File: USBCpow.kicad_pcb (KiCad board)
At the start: 2 copper layers, 16.5 x 12.7 mm, 7 parts, among them CN1 CON_USB-C-6, J1 Conn_01x05, U1 LM1117-3.3

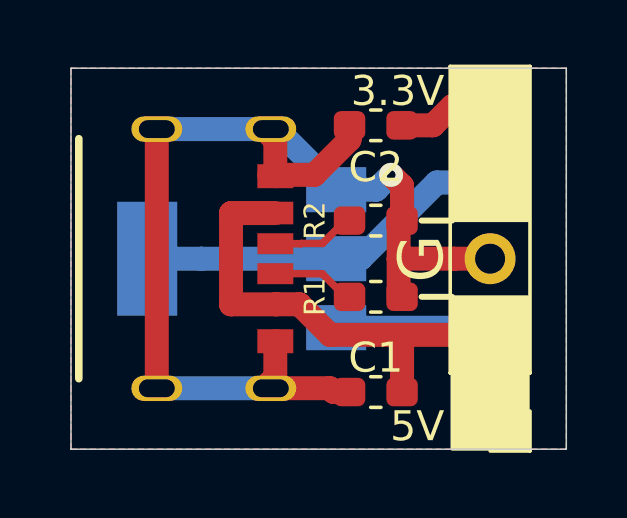
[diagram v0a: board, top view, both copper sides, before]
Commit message: 固定用ピンヘッダの穴を追加
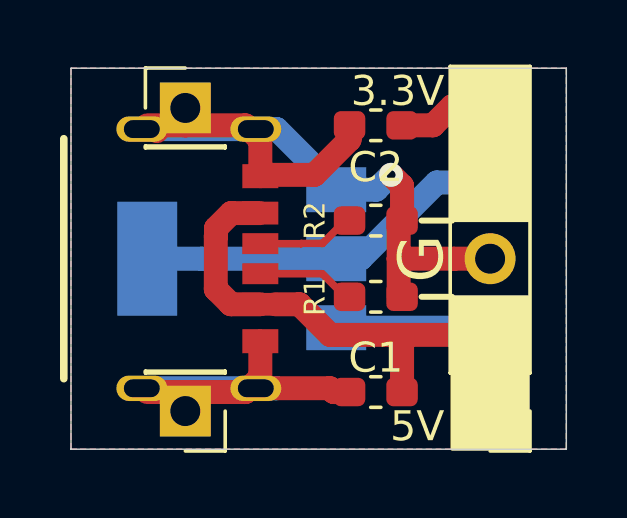
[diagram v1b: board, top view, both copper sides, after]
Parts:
- added J2: Conn_01x01, Connector_PinHeader_2.54mm:PinHeader_1x01_P2.54mm_Vertical, F.Cu at (3.81, -11.4)
- added J3: Conn_01x01, Connector_PinHeader_2.54mm:PinHeader_1x01_P2.54mm_Vertical, F.Cu at (3.81, -1.27)
- moved CN1 0.50 mm to (3.31, -6.35)
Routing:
- net Net-(C1-Pad1): track 25.9 -> 25.3 mm
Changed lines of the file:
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@@
     (thickness 1.6)
     (drawings 22)
-    (tracks 56)
+    (tracks 64)
     (zones 0)
-    (modules 7)
+    (modules 9)
     (nets 6)
   )
@@
   (layers
     (0 F.Cu signal hide)
-    (31 B.Cu signal)
+    (31 B.Cu signal hide)
     (32 B.Adhes user hide)
     (33 F.Adhes user hide)
@@
     (35 F.Paste user)
     (36 B.SilkS user)
-    (37 F.SilkS user)
+    (37 F.SilkS user hide)
     (38 B.Mask user)
-    (39 F.Mask user)
+    (39 F.Mask user hide)
     (44 Edge.Cuts user)
     (45 Margin user hide)
@@
   )
   (setup
-    (last_trace_width 0.25)
+    (last_trace_width 0.8)
     (user_trace_width 0.4)
     (user_trace_width 0.6)
@@
     (add_net "Net-(CN1-PadB5)")
   )
+  (module Connector_PinHeader_2.54mm:PinHeader_1x01_P2.54mm_Vertical (layer F.Cu)
+    (at 3.81 -1.27 180)
+    (descr "Through hole straight pin header, 1x01, 2.54mm pitch, single row")
+    (tags "Through hole pin header THT 1x01 2.54mm single row")
+    (fp_text reference J3 (at 0 -2.33) (layer F.SilkS) hide
+      (effects (font (size 1 1) (thickness 0.15)))
+    )
+    (fp_text value Conn_01x01 (at 0 2.33) (layer F.Fab) hide
+      (effects (font (size 1 1) (thickness 0.15)))
+    )
+    (fp_text user %R (at 0 0 90) (layer F.Fab) hide
+      (effects (font (size 1 1) (thickness 0.15)))
+    )
+    (fp_line (start 1.8 -1.8) (end -1.8 -1.8) (layer F.CrtYd) (width 0.05))
+    (fp_line (start 1.8 1.8) (end 1.8 -1.8) (layer F.CrtYd) (width 0.05))
+    (fp_line (start -1.8 1.8) (end 1.8 1.8) (layer F.CrtYd) (width 0.05))
+    (fp_line (start -1.8 -1.8) (end -1.8 1.8) (layer F.CrtYd) (width 0.05))
+    (fp_line (start -1.33 -1.33) (end 0 -1.33) (layer F.SilkS) (width 0.12))
+    (fp_line (start -1.33 0) (end -1.33 -1.33) (layer F.SilkS) (width 0.12))
+    (fp_line (start -1.33 1.27) (end 1.33 1.27) (layer F.SilkS) (width 0.12))
+    (fp_line (start 1.33 1.27) (end 1.33 1.33) (layer F.SilkS) (width 0.12))
+    (fp_line (start -1.33 1.27) (end -1.33 1.33) (layer F.SilkS) (width 0.12))
+    (fp_line (start -1.33 1.33) (end 1.33 1.33) (layer F.SilkS) (width 0.12))
+    (fp_line (start -1.27 -0.635) (end -0.635 -1.27) (layer F.Fab) (width 0.1))
+    (fp_line (start -1.27 1.27) (end -1.27 -0.635) (layer F.Fab) (width 0.1))
+    (fp_line (start 1.27 1.27) (end -1.27 1.27) (layer F.Fab) (width 0.1))
+    (fp_line (start 1.27 -1.27) (end 1.27 1.27) (layer F.Fab) (width 0.1))
+    (fp_line (start -0.635 -1.27) (end 1.27 -1.27) (layer F.Fab) (width 0.1))
+    (pad 1 thru_hole rect (at 0 0 180) (size 1.7 1.7) (drill 1) (layers *.Cu *.Mask)
+      (net 1 "Net-(C1-Pad2)"))
+    (model ${KISYS3DMOD}/Connector_PinHeader_2.54mm.3dshapes/PinHeader_1x01_P2.54mm_Vertical.wrl
+      (at (xyz 0 0 0))
+      (scale (xyz 1 1 1))
+      (rotate (xyz 0 0 0))
+    )
+  )
+  (module Connector_PinHeader_2.54mm:PinHeader_1x01_P2.54mm_Vertical (layer F.Cu)
+    (at 3.81 -11.374999)
+    (descr "Through hole straight pin header, 1x01, 2.54mm pitch, single row")
+    (tags "Through hole pin header THT 1x01 2.54mm single row")
+    (fp_text reference J2 (at 0 -2.33) (layer F.SilkS) hide
+      (effects (font (size 1 1) (thickness 0.15)))
+    )
+    (fp_text value Conn_01x01 (at 0 2.33) (layer F.Fab) hide
+      (effects (font (size 1 1) (thickness 0.15)))
+    )
+    (fp_text user %R (at 0 0 90) (layer F.Fab) hide
+      (effects (font (size 1 1) (thickness 0.15)))
+    )
+    (fp_line (start 1.8 -1.8) (end -1.8 -1.8) (layer F.CrtYd) (width 0.05))
+    (fp_line (start 1.8 1.8) (end 1.8 -1.8) (layer F.CrtYd) (width 0.05))
+    (fp_line (start -1.8 1.8) (end 1.8 1.8) (layer F.CrtYd) (width 0.05))
+    (fp_line (start -1.8 -1.8) (end -1.8 1.8) (layer F.CrtYd) (width 0.05))
+    (fp_line (start -1.33 -1.33) (end 0 -1.33) (layer F.SilkS) (width 0.12))
+    (fp_line (start -1.33 0) (end -1.33 -1.33) (layer F.SilkS) (width 0.12))
+    (fp_line (start -1.33 1.27) (end 1.33 1.27) (layer F.SilkS) (width 0.12))
+    (fp_line (start 1.33 1.27) (end 1.33 1.33) (layer F.SilkS) (width 0.12))
+    (fp_line (start -1.33 1.27) (end -1.33 1.33) (layer F.SilkS) (width 0.12))
+    (fp_line (start -1.33 1.33) (end 1.33 1.33) (layer F.SilkS) (width 0.12))
+    (fp_line (start -1.27 -0.635) (end -0.635 -1.27) (layer F.Fab) (width 0.1))
+    (fp_line (start -1.27 1.27) (end -1.27 -0.635) (layer F.Fab) (width 0.1))
+    (fp_line (start 1.27 1.27) (end -1.27 1.27) (layer F.Fab) (width 0.1))
+    (fp_line (start 1.27 -1.27) (end 1.27 1.27) (layer F.Fab) (width 0.1))
+    (fp_line (start -0.635 -1.27) (end 1.27 -1.27) (layer F.Fab) (width 0.1))
+    (pad 1 thru_hole rect (at 0 0) (size 1.7 1.7) (drill 1) (layers *.Cu *.Mask)
+      (net 1 "Net-(C1-Pad2)"))
+    (model ${KISYS3DMOD}/Connector_PinHeader_2.54mm.3dshapes/PinHeader_1x01_P2.54mm_Vertical.wrl
+      (at (xyz 0 0 0))
+      (scale (xyz 1 1 1))
+      (rotate (xyz 0 0 0))
+    )
+  )
   (module Connector_PinHeader_2.54mm:PinHeader_1x05_P2.54mm_Vertical (layer F.Cu)
     (at 13.97 -1.27 180)
@@
     (tags "CMS SOT")
     (attr smd)
-    (fp_text reference U1 (at 3.785 2.54) (layer B.SilkS)
+    (fp_text reference U1 (at 3.15 2.794) (layer B.SilkS)
       (effects (font (size 1 1) (thickness 0.15)) (justify mirror))
     )
@@
   )
   (module akita:USB-C_6P (layer F.Cu)
-    (at 3.81 -6.35 270)
+    (at 3.31 -6.35 270)
     (descr "USB TypeC Receptacle, 6p (with 18p dummy), no D+/D-")
     (attr smd)
@@
     (effects (font (size 1 1) (thickness 0.2)) (justify right))
   )
-  (gr_text USBCpow (at 6.604 -11.938) (layer B.SilkS)
+  (gr_text USBCpow (at 0.762 -6.35 90) (layer B.SilkS)
     (effects (font (size 0.8 0.8) (thickness 0.2)) (justify mirror))
   )
@@
     (effects (font (size 1.5 1.5) (thickness 0.3)) (justify mirror))
   )
-  (gr_text @akita11 (at 6.604 -0.762) (layer B.SilkS)
+  (gr_text @akita11 (at 7.62 -0.635) (layer B.SilkS)
     (effects (font (size 0.7 0.7) (thickness 0.15)) (justify mirror))
   )
@@
     (effects (font (size 1 1) (thickness 0.2)) (justify right))
   )
-  (segment (start 6.81 -10.3) (end 6.604 -10.506) (width 0.8) (layer F.Cu) (net 1))
-  (segment (start 6.81 -9.1) (end 6.81 -10.3) (width 0.8) (layer F.Cu) (net 1))
-  (segment (start 6.81 -2.4) (end 6.604 -2.194) (width 0.8) (layer F.Cu) (net 1))
-  (segment (start 6.81 -3.6) (end 6.81 -2.4) (width 0.8) (layer F.Cu) (net 1))
-  (segment (start 6.604 -2.194) (end 6.604 -2.032) (width 0.8) (layer F.Cu) (net 1))
   (segment (start 2.86 -10.67) (end 6.856 -10.67) (width 0.8) (layer B.Cu) (net 1))
   (segment (start 6.856 -10.67) (end 8.89 -8.636) (width 0.8) (layer B.Cu) (net 1))
   (segment (start 2.86 -2.03) (end 6.856 -2.03) (width 0.8) (layer B.Cu) (net 1))
   (segment (start 6.856 -2.03) (end 6.858 -2.032) (width 0.8) (layer B.Cu) (net 1))
-  (segment (start 2.86 -2.03) (end 2.86 -10.602) (width 0.8) (layer F.Cu) (net 1))
   (segment (start 2.86 -10.602) (end 2.794 -10.668) (width 0.8) (layer F.Cu) (net 1))
   (segment (start 9.285 -10.32) (end 8.109 -9.144) (width 0.8) (layer F.Cu) (net 1))
@@
   (segment (start 9.285 -1.905) (end 8.76 -1.905) (width 0.8) (layer F.Cu) (net 1))
   (segment (start 8.633 -2.032) (end 6.604 -2.032) (width 0.8) (layer F.Cu) (net 1))
-  (segment (start 6.81 -7.87) (end 5.338 -7.87) (width 0.8) (layer F.Cu) (net 2))
-  (segment (start 5.338 -7.87) (end 5.334 -7.866) (width 0.8) (layer F.Cu) (net 2))
-  (segment (start 5.334 -7.866) (end 5.334 -4.826) (width 0.8) (layer F.Cu) (net 2))
-  (segment (start 5.334 -4.826) (end 6.858 -4.826) (width 0.8) (layer F.Cu) (net 2))
+  (segment (start 6.16 -10.67) (end 6.225 -10.67) (width 0.8) (layer F.Cu) (net 1))
+  (segment (start 6.31 -10.3) (end 5.815 -10.795) (width 0.8) (layer F.Cu) (net 1))
+  (segment (start 6.31 -9.1) (end 6.31 -10.3) (width 0.8) (layer F.Cu) (net 1))
+  (segment (start 3.81 -11.374999) (end 3.81 -10.795) (width 0.8) (layer F.Cu) (net 1))
+  (segment (start 5.815 -10.795) (end 3.81 -10.795) (width 0.8) (layer F.Cu) (net 1))
+  (segment (start 3.81 -10.795) (end 2.54 -10.795) (width 0.8) (layer F.Cu) (net 1))
+  (segment (start 6.31 -2.4) (end 5.815 -1.905) (width 0.8) (layer F.Cu) (net 1))
+  (segment (start 6.31 -3.6) (end 6.31 -2.4) (width 0.8) (layer F.Cu) (net 1))
+  (segment (start 3.81 -1.27) (end 3.81 -1.905) (width 0.8) (layer F.Cu) (net 1))
+  (segment (start 5.815 -1.905) (end 3.81 -1.905) (width 0.8) (layer F.Cu) (net 1))
+  (segment (start 3.81 -1.905) (end 2.54 -1.905) (width 0.8) (layer F.Cu) (net 1))
   (segment (start 13.73 -4.05) (end 13.97 -3.81) (width 0.8) (layer B.Cu) (net 2))
   (segment (start 8.84 -4.05) (end 13.73 -4.05) (width 0.8) (layer B.Cu) (net 2))
@@
   (segment (start 13.97 -3.81) (end 13.97 -1.27) (width 1.2) (layer F.Cu) (net 2))
   (segment (start 13.97 -3.81) (end 13.97 -1.27) (width 1.2) (layer B.Cu) (net 2))
+  (segment (start 6.31 -4.83) (end 5.33 -4.83) (width 0.8) (layer F.Cu) (net 2))
+  (segment (start 5.33 -4.83) (end 4.826 -5.334) (width 0.8) (layer F.Cu) (net 2))
+  (segment (start 4.826 -5.334) (end 4.826 -7.112) (width 0.8) (layer F.Cu) (net 2))
+  (segment (start 4.834 -7.112) (end 4.826 -7.112) (width 0.8) (layer F.Cu) (net 2))
+  (segment (start 6.31 -7.87) (end 5.338 -7.87) (width 0.8) (layer F.Cu) (net 2))
+  (segment (start 4.834 -7.366) (end 4.834 -7.112) (width 0.8) (layer F.Cu) (net 2))
+  (segment (start 5.338 -7.87) (end 4.834 -7.366) (width 0.8) (layer F.Cu) (net 2))
   (segment (start 2.54 -6.35) (end 4.34 -6.35) (width 0.8) (layer B.Cu) (net 3))
   (segment (start 4.34 -6.35) (end 8.89 -6.35) (width 0.8) (layer B.Cu) (net 3))
